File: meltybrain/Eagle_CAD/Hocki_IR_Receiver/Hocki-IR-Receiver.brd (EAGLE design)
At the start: 42 x 34 mm, 68 parts, among them J1 SM03B-SRSS-TB(LF)(SN), U1 OPA2380AIDGKR, U10 LMH6612MAX/NOPB, U11 LMH6612MAX/NOPB, U2 OPA2380AIDGKR, U3 TLV3502AIDCNR, U4 TLV3502AIDCNR, U5 SN74LVC1G58DCKR, U6 NL27WZ32USG, U7 TMUX1204DGSR, U8 AP2210K-5.0TRG1, U9 TLV73310PDBVT

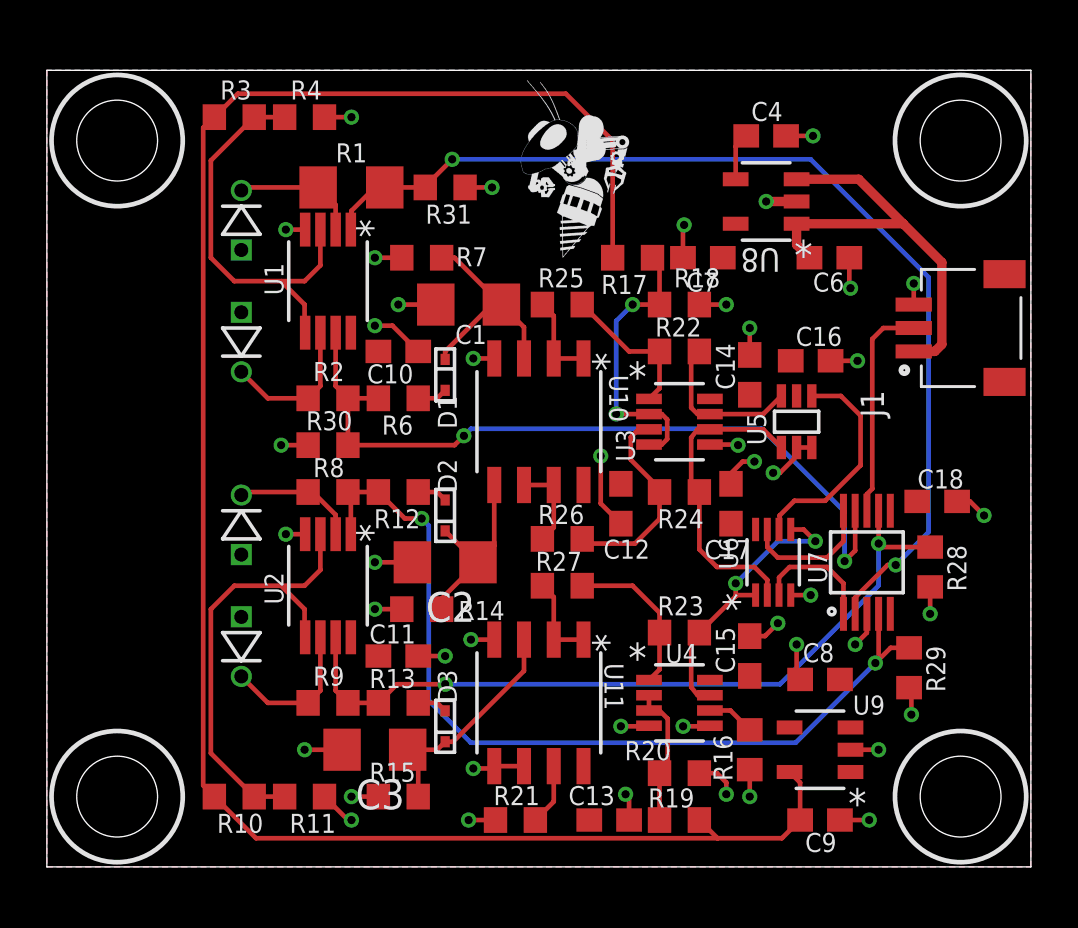
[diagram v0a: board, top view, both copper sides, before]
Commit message: Made board 1mm larger and moved LEDs to help with mounting
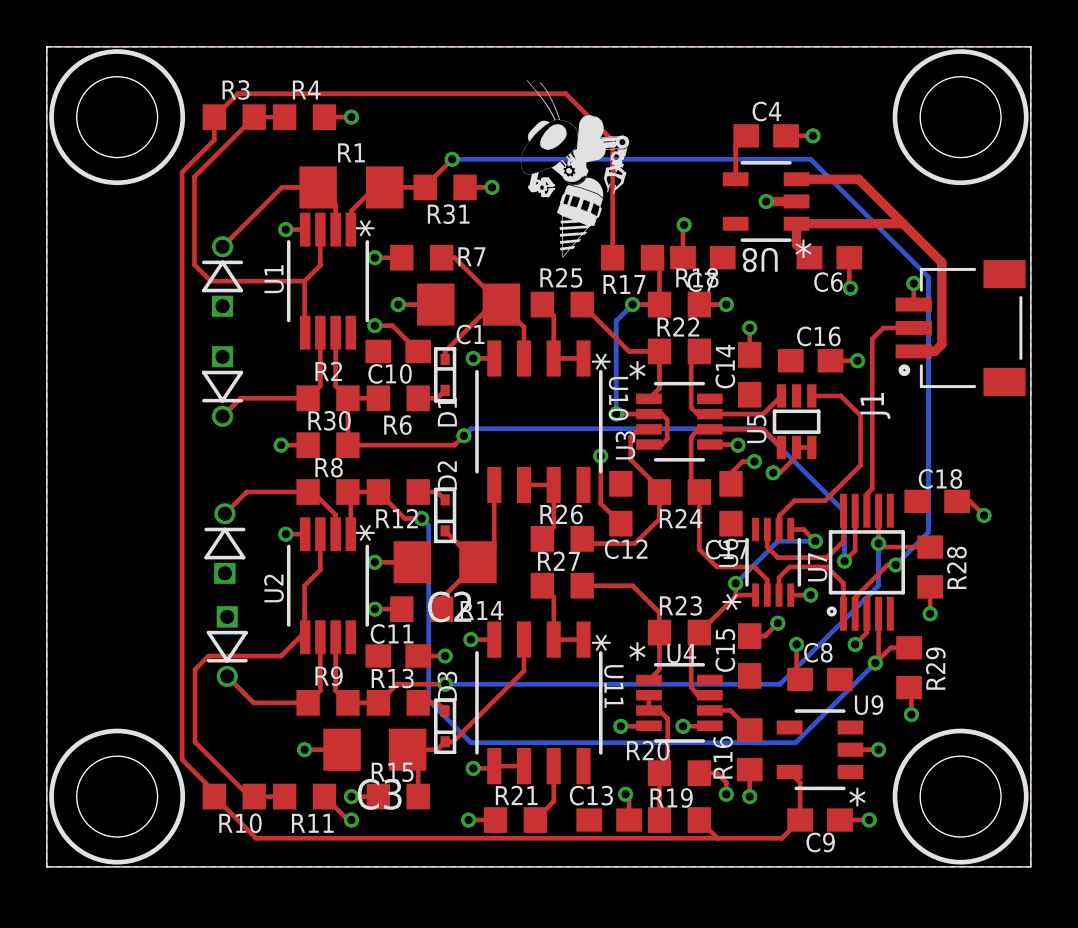
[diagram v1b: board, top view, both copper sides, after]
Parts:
- moved D4 2.53 mm to (7.50, 25.2)
- moved D5 2.06 mm to (7.50, 20.5)
- moved D6 1.06 mm to (7.60, 13.8)
- moved D7 0.60 mm to (7.70, 9.40)
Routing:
- net N$1: track 5.44 -> 7.24 mm
- net N$12: track 19.6 -> 17.9 mm
- net N$6: track 5.31 -> 6.34 mm
- net N$5: track 17.6 -> 18.3 mm
- net 1.0V: track 82.0 -> 82.8 mm
- net N$3: track 6.34 -> 6.99 mm
- net N$10: track 6.34 -> 6.94 mm
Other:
- board size 42 x 34 mm -> 42 x 35 mm

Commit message: IR board 100%...again
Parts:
- removed C18: 0.1u, rcl:C0603
- added C5: 47nF, rcl:C1206
- added D8, D9: GREEN, SparkFun-LED:LED-0603
- added R32: 300, resistor:R0603
- added R5: 10M, rcl:R1206
- C1, C2: value 47n -> 1uF; device rcl:C1206 -> rcl:C0603
- C10: value 1u -> 2.2uF
- C11, C6: value 1u -> 1uF
- C12: value 0.1u -> 1uF
- C13, C14, C15, C16, C17: value 0.1u -> 0.1uF
- C3: value 47n -> 47nF
- C4: value 100p -> 47nF; device rcl:C0603 -> rcl:C1206
- C7: value 2.2u -> 100pF
- C8, C9: value 1u -> 0.1uF
- D1, D2, D3: value RB521S30T1G -> TEFD4300F; device Hocki_Library:SOD-523 -> Hocki_Library:TEFD4300F
- D5, D6, D7: value TEFD4300F -> RB521S30T1G; device Hocki_Library:TEFD4300F -> Hocki_Library:SOD-523
- R1: value 10M -> 499; device rcl:R1206 -> resistor:R0603
- R10, R11: value 499 -> 49.9
- R12, R13: value 50 -> 31.6k
- R15: value 31.6k -> 499
- R16: value 499 -> 100
- R17: value 100 -> 30
- R18: value 300 -> 30
- R19: value 100 -> 300
- R2: value 1M -> 499
- R20: value 300 -> 100
- R21: value 499 -> 30
- R22: value 10k -> 300
- R25: value 30 -> 10k
- R26, R27: value 30 -> 499
- R6: value 50 -> 1M
- R7: value 31.6k -> 100k
- R8: value 100k -> 10k
- R9: value 10k -> 49.9
- U10: value LMH6612MAX/NOPB -> NL27WZ32USG; device Hocki_Library:8-SOIC -> Hocki_Library:US8
- U11: value LMH6612MAX/NOPB -> TMUX1204DGSR; device Hocki_Library:8-SOIC -> Hocki_Library:10-VSSOP
- U3: value TLV3502AIDCNR -> AP2210K-5.0TRG1; device Hocki_Library:SOT-23-8 -> Hocki_Library:SOT-23-5
- U4: value TLV3502AIDCNR -> LMH6612MAX/NOPB; device Hocki_Library:SOT-23-8 -> Hocki_Library:8-SOIC
- U5: value SN74LVC1G58DCKR -> LMH6612MAX/NOPB; device Hocki_Library:SC-70-6 -> Hocki_Library:8-SOIC
- U6: value NL27WZ32USG -> TLV73310PDBVT; device Hocki_Library:US8 -> Hocki_Library:SOT-23-5
- U7: value TMUX1204DGSR -> TLV3502AIDCNR; device Hocki_Library:10-VSSOP -> Hocki_Library:SOT-23-8
- U8: value AP2210K-5.0TRG1 -> TLV3502AIDCNR; device Hocki_Library:SOT-23-5 -> Hocki_Library:SOT-23-8
- U9: value TLV73310PDBVT -> SN74LVC1G58DCKR; device Hocki_Library:SOT-23-5 -> Hocki_Library:SC-70-6
- moved R3 29.0 mm to (8.00, 3.00)
- moved R4 29.0 mm to (11.0, 3.00)
- moved R28 26.2 mm to (12.0, 18.0), turned to 0 degrees
- moved R30 26.2 mm to (37.7, 12.8), turned to 90 degrees
- moved R31 24.2 mm to (38.5, 18.0)
- moved C4 22.8 mm to (17.0, 13.0), turned to 180 degrees
- moved R20 22.1 mm to (25.0, 26.0)
- moved U8 21.7 mm to (27.0, 7.00), turned to 0 degrees
- moved C13 19.9 mm to (30.0, 21.0), turned to 90 degrees
- moved C3 19.4 mm to (18.0, 24.0)
- moved C11 18.0 mm to (33.0, 8.00), turned to 180 degrees
- moved R27 17.7 mm to (17.0, 29.0), turned to 180 degrees
- moved D3 17.3 mm to (7.50, 20.5), flipped to the bottom, turned to 270 degrees
- moved U5 16.3 mm to (21.0, 7.00), turned to 270 degrees
- moved C12 16.0 mm to (33.0, 2.00), turned to 0 degrees
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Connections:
- new net N$11: D9.C, R32.2
- new net N$24: D8.C, R31.2
- net 1.0V: now also C12.1, R1.2, R16.2, R20.2, U6.5; no longer C9.1, R10.2, R17.2, R19.2, U9.5
- net 100KGAIN: now also R11.1, R7.2, U11.4; no longer R12.1, R8.2, U7.4
- net 100KLOGIC: now also U10.2, U7.6, U9.1; no longer U3.6, U5.1, U6.2
- net 100KPEAK: now also C4.1, D6.1, R13.2, U4.5; no longer C2.1, D2.1, R14.2, U10.5
- net 10KGAIN: now also R10.1, R30.2, R8.2, U11.7; no longer R13.1, R28.2, R9.2, U7.7
- net 10KLOGIC: now also R25.1, U10.1, U10.5, U8.7; no longer R23.1, U4.7, U6.1, U6.5
- net 10KPEAK: now also C5.1, D7.1, R14.2, U5.3; no longer C3.1, D3.1, R15.2, U11.3
- net 10MGAIN: now also R27.2, R5.2, U11.2; no longer R1.2, R31.2, U7.2
- net 1MGAIN: now also R28.2, R6.2, R9.1, U11.9; no longer R2.2, R30.2, R6.1, U7.9
- net 1MLOGIC: now also R23.1, U7.7, U9.6; no longer R22.1, U3.7, U5.6
- net 5V: now also C1.1, C2.1, C9.1, D9.A, U11.5, U11.6, U3.5, U5.8, U6.1, U6.3, U7.8, U8.8, U9.5; no longer C12.1, C18.1, C7.1, U11.8, U3.8, U5.5, U6.8, U7.5, U7.6, U8.5, U9.1, U9.3
- net 9V: now also D8.A, U3.1, U3.3; no longer U8.1, U8.3
- net A0: now also U10.3, U11.1; no longer U6.3, U7.1
- net A1: now also U10.7, U11.10; no longer U6.7, U7.10
- net GND: now also C5.2, D1.1, D2.1, D3.1, R12.1, R13.1, R19.1, R2.1, R22.1, R26.1, R27.1, R32.1, U11.3, U3.2, U5.4, U5.5, U5.6, U6.2, U7.5, U8.4, U8.5, U9.3; no longer C18.2, D5.1, D6.1, D7.1, R11.1, R16.1, R18.1, R20.1, R21.1, R7.1, U11.4, U11.5, U11.6, U3.5, U4.5, U5.2, U5.3, U6.4, U7.3, U8.2
- net N$1: now also D1.2, R5.1; no longer D4.2, R1.1
- net N$10: now also D4.2, R8.1; no longer D7.2, R9.1
- net N$12: now also R3.1, R4.2; no longer R10.1, R11.2
- net N$13: now also R20.1, R22.2, U7.2, U7.4; no longer R17.1, R18.2, U3.2, U3.4
- net N$14: now also R16.1, R19.2, U8.2, U8.3; no longer R19.1, R20.2, U4.2, U4.3
- net N$15: now also R21.1, U5.1, U5.2; no longer R27.1, U11.1, U11.2
- net N$16: now also R17.1, U4.1, U4.2; no longer R25.1, U10.1, U10.2
- net N$17: now also C3.1, D5.1, R12.2, U4.3; no longer C1.1, D1.1, R7.2, U10.3
- net N$18: now also R18.1, U4.6, U4.7; no longer R26.1, U10.6, U10.7
- net N$19: now also R15.2, U5.7; no longer R21.2, U11.7
- net N$2: now also D6.2, R11.2; no longer D2.2, R12.2
- net N$20: now also R18.2, U7.3; no longer R26.2, U3.3
- net N$21: now also D5.2, R9.2; no longer D1.2, R6.2
- net N$22: now also R21.2, R25.2, U8.1; no longer R23.2, R27.2, U4.1
- net N$23: now also R17.2, R23.2, U7.1; no longer R22.2, R25.2, U3.1
- net N$3: now also D3.2, R6.1; no longer D5.2, R2.1
- net N$4: now also D7.2, R10.2; no longer D3.2, R13.2
- net N$5: now also R1.1, R2.2; no longer R3.1, R4.2
- net N$6: now also D2.2, R7.1; no longer D6.2, R8.1
- net N$7: now also R26.2, U8.6; no longer R16.2, U4.6
- net N$8: now also C7.1, U3.4; no longer C4.1, U8.4
- net N$9: now also U10.6, U9.4; no longer U5.4, U6.6
- net VG_SIGNAL: now also U11.8; no longer U7.8
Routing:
- net 9V: track 18.7 -> 21.4 mm
- net GND: track 59.6 -> 62.1 mm, vias 44 -> 46
- net N$11: track 0.00 -> 1.77 mm
- net N$24: track 0.00 -> 1.66 mm
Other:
- board text added: "5V"
- board text added: "9V"
- board text added: "Hocki"

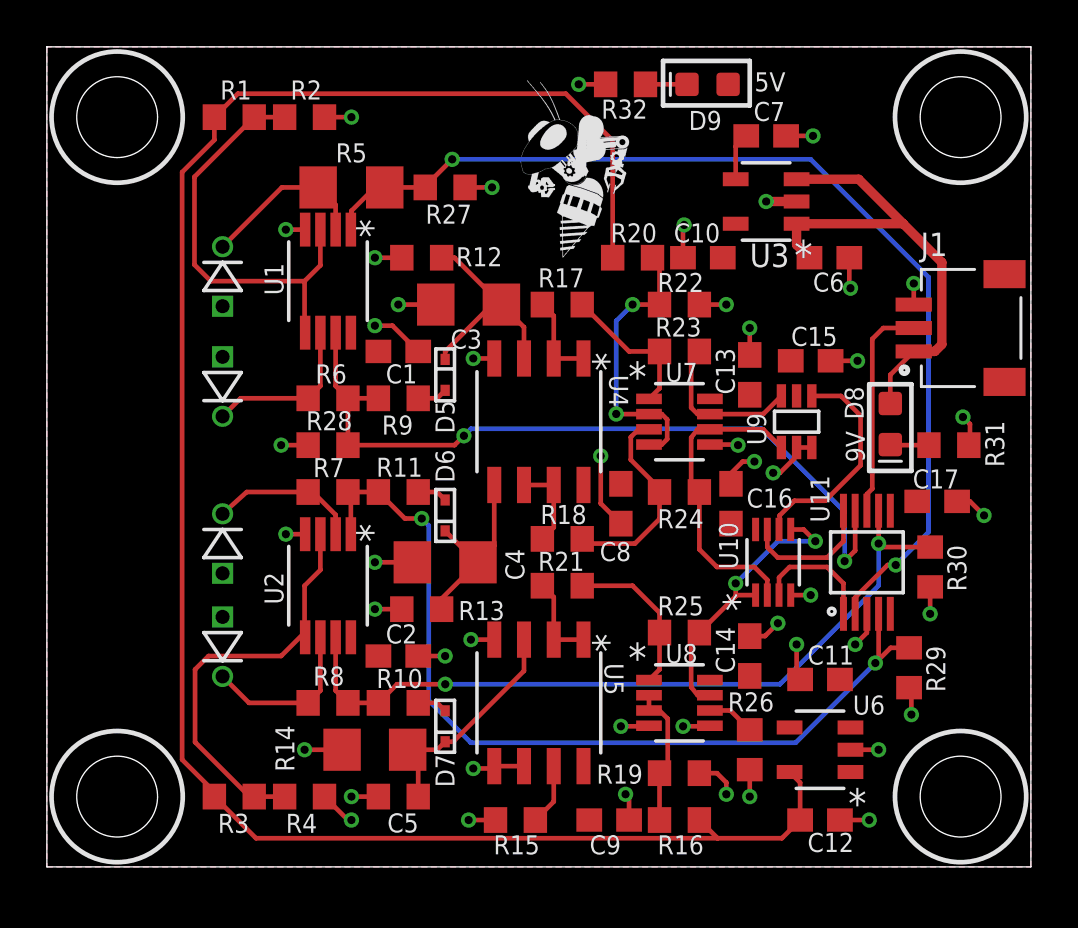
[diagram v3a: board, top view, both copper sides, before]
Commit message: IR Receiver schematic edits. Added ldo protection
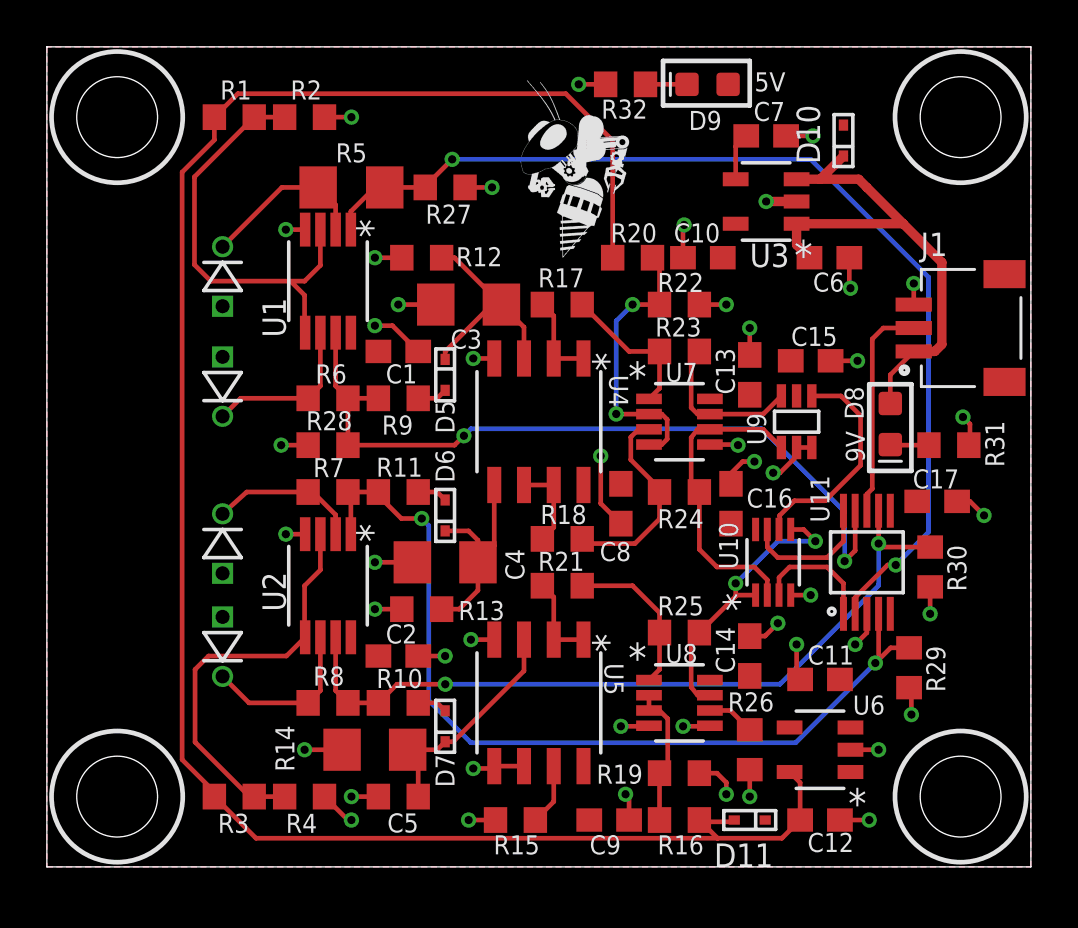
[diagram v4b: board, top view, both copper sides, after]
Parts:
- added D10, D11: BAS581-02V-V-G-08, Hocki_Library:SOD-523
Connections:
- net N$15 renamed 10KPEAK_BUF
- net N$16 renamed 1MPEAK_BUF
- net N$17 renamed 1MPEAK
- net N$18 renamed 100KPEAK_BUF
- net 1.0V: now also D11.2
- net 5V: now also D10.2, D11.1
- net 9V: now also D10.1
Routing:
- net 1.0V: track 82.8 -> 84.2 mm
- net 9V: track 21.4 -> 22.8 mm
- net 100KPEAK: track 8.18 -> 9.17 mm

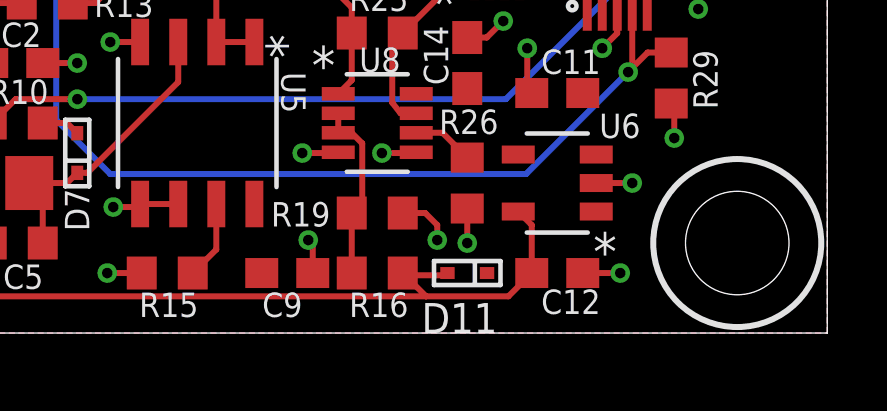
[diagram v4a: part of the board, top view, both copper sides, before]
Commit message: Edited silkscreen and made minor changes to IR Receiver silkscreen and schematic
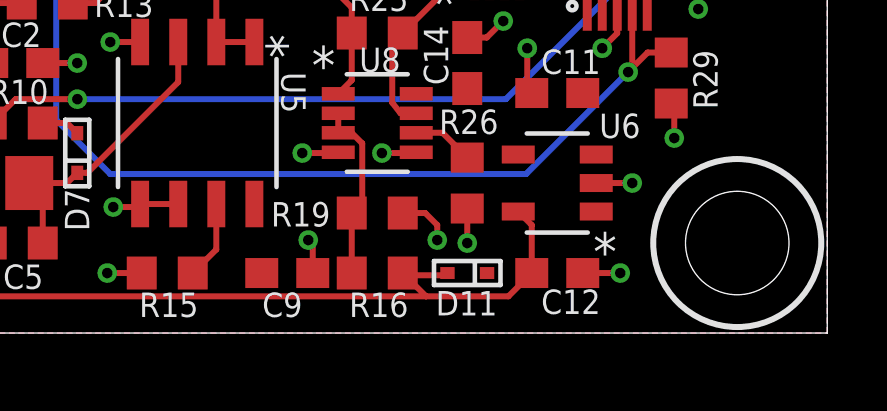
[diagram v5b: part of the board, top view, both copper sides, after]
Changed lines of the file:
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@@
 <drawing>
 <settings>
-<setting alwaysvectorfont="no"/>
+<setting alwaysvectorfont="yes"/>
 <setting verticaltext="up"/>
 </settings>
@@
 <element name="D11" library="Hocki_Library" package="SOD-523" value="BAS581-02V-V-G-08" x="30" y="2" smashed="yes" rot="R180">
 <attribute name="DKPN" value="112-BAS581-02V-V-G-08CT-ND" x="30" y="2" size="1.778" layer="27" rot="R180" display="off"/>
-<attribute name="NAME" x="31" y="1" size="1" layer="25" font="vector" rot="R180"/>
+<attribute name="NAME" x="31" y="1.4" size="0.8128" layer="25" font="vector" rot="R180"/>
 <attribute name="VALUE" x="31" y="3" size="1" layer="27" font="vector" rot="R180" align="top-left"/>
 </element>

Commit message: comparator trigger point fixed
assumed diode voltage drop was constant originally
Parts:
- R16, R20: value 100 -> 49.9
- R19, R22: value 300 -> 499
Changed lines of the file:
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@@
 <drawing>
 <settings>
-<setting alwaysvectorfont="yes"/>
+<setting alwaysvectorfont="no"/>
 <setting verticaltext="up"/>
 </settings>
@@
 <attribute name="VALUE" x="31.905" y="4.365" size="1.27" layer="27" rot="R90"/>
 </element>
-<element name="R20" library="resistor" library_urn="urn:adsk.eagle:library:348" package="R0603" package3d_urn="urn:adsk.eagle:package:26057/1" value="100" x="25" y="26" smashed="yes" rot="R180">
+<element name="R20" library="resistor" library_urn="urn:adsk.eagle:library:348" package="R0603" package3d_urn="urn:adsk.eagle:package:26057/1" value="49.9" x="25" y="26" smashed="yes" rot="R180">
 <attribute name="NAME" x="26.035" y="27.465" size="0.8128" layer="25" font="vector" rot="R180"/>
 <attribute name="VALUE" x="25.635" y="27.905" size="1.27" layer="27" rot="R180"/>
 </element>
-<element name="R22" library="resistor" library_urn="urn:adsk.eagle:library:348" package="R0603" package3d_urn="urn:adsk.eagle:package:26057/1" value="300" x="27" y="24" smashed="yes" rot="R180">
+<element name="R22" library="resistor" library_urn="urn:adsk.eagle:library:348" package="R0603" package3d_urn="urn:adsk.eagle:package:26057/1" value="499" x="27" y="24" smashed="yes" rot="R180">
 <attribute name="NAME" x="26.065" y="24.535" size="0.8128" layer="25" font="vector"/>
 <attribute name="VALUE" x="27.635" y="25.905" size="1.27" layer="27" rot="R180"/>
 </element>
-<element name="R16" library="resistor" library_urn="urn:adsk.eagle:library:348" package="R0603" package3d_urn="urn:adsk.eagle:package:26057/1" value="100" x="27" y="2" smashed="yes">
+<element name="R16" library="resistor" library_urn="urn:adsk.eagle:library:348" package="R0603" package3d_urn="urn:adsk.eagle:package:26057/1" value="49.9" x="27" y="2" smashed="yes">
 <attribute name="NAME" x="26.065" y="0.535" size="0.8128" layer="25" font="vector"/>
 <attribute name="VALUE" x="26.365" y="0.095" size="1.27" layer="27"/>
@@
 <attribute name="VALUE" x="11.365" y="18.095" size="1.27" layer="27"/>
 </element>
-<element name="R19" library="resistor" library_urn="urn:adsk.eagle:library:348" package="R0603" package3d_urn="urn:adsk.eagle:package:26057/1" value="300" x="27" y="4" smashed="yes" rot="R180">
+<element name="R19" library="resistor" library_urn="urn:adsk.eagle:library:348" package="R0603" package3d_urn="urn:adsk.eagle:package:26057/1" value="499" x="27" y="4" smashed="yes" rot="R180">
 <attribute name="NAME" x="25.435" y="4.365" size="0.8128" layer="25" font="vector" rot="R180"/>
 <attribute name="VALUE" x="27.635" y="5.905" size="1.27" layer="27" rot="R180"/>
